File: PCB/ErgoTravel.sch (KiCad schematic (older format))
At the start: 63 parts, among them J1 Conn_01x03, J2 Audio-Jack-4, J3 Audio-Jack-4, K1 KEYSW, K10 KEYSW, K11 KEYSW, K12 KEYSW, K13 KEYSW, K14 KEYSW, K15 KEYSW, K16 KEYSW, K17 KEYSW, K18 KEYSW, K19 KEYSW, K2 KEYSW, K20 KEYSW, K21 KEYSW, K22 KEYSW, K23 KEYSW, K24 KEYSW, K25 KEYSW, K26 KEYSW, K27 KEYSW, K28 KEYSW, K3 KEYSW, K4 KEYSW, K5 KEYSW, K6 KEYSW, K7 KEYSW, K8 KEYSW, K9 KEYSW, SW1 SW_PUSH, SW2 SW_PUSH, U1 ProMicro

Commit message: Adding internal Plates
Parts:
- added J4: Conn_01x06, footprints:ICSP-Header, symbol Conn_01x06
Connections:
- net labels added: MISO, MOSI, RESET, SCK
- wire segments 172 -> 186
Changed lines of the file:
@@
 LIBS:keyboard_parts
 LIBS:canadian_parts
+LIBS:ErgoTravel-cache
 EELAYER 25 0
 EELAYER END
@@
 L GND #PWR06
 U 1 1 5A9D5401
-P 7100 4700
-F 0 "#PWR06" H 7100 4450 50  0001 C CNN
-F 1 "GND" H 7100 4550 50  0000 C CNN
-F 2 "" H 7100 4700 50  0001 C CNN
-F 3 "" H 7100 4700 50  0001 C CNN
-	1    7100 4700
+P 7350 4200
+F 0 "#PWR06" H 7350 3950 50  0001 C CNN
+F 1 "GND" H 7350 4050 50  0000 C CNN
+F 2 "" H 7350 4200 50  0001 C CNN
+F 3 "" H 7350 4200 50  0001 C CNN
+	1    7350 4200
 	0    1    1    0
 $EndComp
@@
 L GND #PWR07
 U 1 1 5A9D54C0
-P 7100 5850
-F 0 "#PWR07" H 7100 5600 50  0001 C CNN
-F 1 "GND" H 7100 5700 50  0000 C CNN
-F 2 "" H 7100 5850 50  0001 C CNN
-F 3 "" H 7100 5850 50  0001 C CNN
-	1    7100 5850
+P 7400 5400
+F 0 "#PWR07" H 7400 5150 50  0001 C CNN
+F 1 "GND" H 7400 5250 50  0000 C CNN
+F 2 "" H 7400 5400 50  0001 C CNN
+F 3 "" H 7400 5400 50  0001 C CNN
+	1    7400 5400
 	0    1    1    0
 $EndComp
@@
 L VCC #PWR08
 U 1 1 5A9D557F
-P 7100 4600
-F 0 "#PWR08" H 7100 4450 50  0001 C CNN
-F 1 "VCC" H 7100 4750 50  0000 C CNN
-F 2 "" H 7100 4600 50  0001 C CNN
-F 3 "" H 7100 4600 50  0001 C CNN
-	1    7100 4600
+P 7350 4800
+F 0 "#PWR08" H 7350 4650 50  0001 C CNN
+F 1 "VCC" H 7350 4950 50  0000 C CNN
+F 2 "" H 7350 4800 50  0001 C CNN
+F 3 "" H 7350 4800 50  0001 C CNN
+	1    7350 4800
 	0    -1   -1   0
 $EndComp
@@
 L VCC #PWR09
 U 1 1 5A9D563E
-P 7100 5750
-F 0 "#PWR09" H 7100 5600 50  0001 C CNN
-F 1 "VCC" H 7100 5900 50  0000 C CNN
-F 2 "" H 7100 5750 50  0001 C CNN
-F 3 "" H 7100 5750 50  0001 C CNN
-	1    7100 5750
-	0    -1   -1   0
-$EndComp
-Text GLabel 7350 4200 0    60   Input ~ 0
+P 7350 5950
+F 0 "#PWR09" H 7350 5800 50  0001 C CNN
+F 1 "VCC" H 7350 6100 50  0000 C CNN
+F 2 "" H 7350 5950 50  0001 C CNN
+F 3 "" H 7350 5950 50  0001 C CNN
+	1    7350 5950
+	0    -1   -1   0
+$EndComp
+Text GLabel 7100 4600 0    60   Input ~ 0
 sda
-Text GLabel 7400 5400 0    60   Input ~ 0
+Text GLabel 7100 5750 0    60   Input ~ 0
 sda
-Text GLabel 7350 4800 0    60   Input ~ 0
+Text GLabel 7100 4700 0    60   Input ~ 0
 scl
-Text GLabel 7350 5950 0    60   Input ~ 0
+Text GLabel 7100 5850 0    60   Input ~ 0
 scl
 $Comp
@@
 Wire Wire Line
 	5350 4650 5650 4650
+$Comp
+L Conn_01x06 J4
+U 1 1 5ABA3EE2
+P 4050 4600
+F 0 "J4" H 4050 4900 50  0000 C CNN
+F 1 "Conn_01x06" H 4050 4200 50  0000 C CNN
+F 2 "footprints:ICSP-Header" H 4050 4600 50  0001 C CNN
+F 3 "" H 4050 4600 50  0001 C CNN
+	1    4050 4600
+	1    0    0    -1
+$EndComp
+$Comp
+L VCC #PWR014
+U 1 1 5ABA3FE3
+P 3750 4500
+F 0 "#PWR014" H 3750 4350 50  0001 C CNN
+F 1 "VCC" H 3750 4650 50  0000 C CNN
+F 2 "" H 3750 4500 50  0001 C CNN
+F 3 "" H 3750 4500 50  0001 C CNN
+	1    3750 4500
+	0    -1   -1   0
+$EndComp
+$Comp
+L GND #PWR015
+U 1 1 5ABA4377
+P 3750 4900
+F 0 "#PWR015" H 3750 4650 50  0001 C CNN
+F 1 "GND" H 3750 4750 50  0000 C CNN
+F 2 "" H 3750 4900 50  0001 C CNN
+F 3 "" H 3750 4900 50  0001 C CNN
+	1    3750 4900
+	0    1    1    0
+$EndComp
+Text GLabel 3500 4800 0    60   Input ~ 0
+RESET
+Text GLabel 4850 5250 2    60   Input ~ 0
+RESET
+Wire Wire Line
+	4850 5250 4500 5250
+Wire Wire Line
+	4500 5250 4500 5700
+Connection ~ 4500 5700
+Wire Wire Line
+	3750 4900 3850 4900
+Wire Wire Line
+	3850 4800 3500 4800
+Wire Wire Line
+	3750 4500 3850 4500
+Text GLabel 3550 4400 0    60   Input ~ 0
+MISO
+Text GLabel 3550 4600 0    60   Input ~ 0
+SCK
+Text GLabel 3550 4700 0    60   Input ~ 0
+MOSI
+Text GLabel 4000 6800 2    60   Input ~ 0
+SCK
+Text GLabel 4000 6950 2    60   Input ~ 0
+MOSI
+Text GLabel 4000 7100 2    60   Input ~ 0
+MISO
+Wire Wire Line
+	4000 6800 3900 6800
+Wire Wire Line
+	3900 6800 3900 6300
+Connection ~ 3900 6300
+Wire Wire Line
+	4000 6950 3850 6950
+Wire Wire Line
+	3850 6950 3850 6500
+Connection ~ 3850 6500
+Wire Wire Line
+	4000 7100 3800 7100
+Wire Wire Line
+	3800 7100 3800 6400
+Connection ~ 3800 6400
+Wire Wire Line
+	3550 4700 3850 4700
+Wire Wire Line
+	3850 4600 3550 4600
+Wire Wire Line
+	3550 4400 3850 4400
 $EndSCHEMATC

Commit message: moved D13
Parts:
- R1, R2: footprint Resistors_Universal:Resistor_SMD+THTuniversal_0805to1206_RM10_HandSoldering_RevA_Date25Jun2010 -> Resistors_THT:R_Axial_DIN0207_L6.3mm_D2.5mm_P10.16mm_Horizontal
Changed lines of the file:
@@
 F 0 "R1" V 9780 4600 50  0000 C CNN
 F 1 "4.7k" V 9700 4600 50  0000 C CNN
-F 2 "Resistors_Universal:Resistor_SMD+THTuniversal_0805to1206_RM10_HandSoldering_RevA_Date25Jun2010" V 9630 4600 50  0001 C CNN
+F 2 "Resistors_THT:R_Axial_DIN0207_L6.3mm_D2.5mm_P10.16mm_Horizontal" V 9630 4600 50  0001 C CNN
 F 3 "" H 9700 4600 50  0001 C CNN
 	1    9700 4600
@@
 F 0 "R2" V 10380 4600 50  0000 C CNN
 F 1 "4.7k" V 10300 4600 50  0000 C CNN
-F 2 "Resistors_Universal:Resistor_SMD+THTuniversal_0805to1206_RM10_HandSoldering_RevA_Date25Jun2010" V 10230 4600 50  0001 C CNN
+F 2 "Resistors_THT:R_Axial_DIN0207_L6.3mm_D2.5mm_P10.16mm_Horizontal" V 10230 4600 50  0001 C CNN
 F 3 "" H 10300 4600 50  0001 C CNN
 	1    10300 4600

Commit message: V1.01 PCB and Plates incl Gerbers
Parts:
- removed J1: Conn_01x03, Pin_Headers:Pin_Header_Straight_1x03_Pitch2.54mm, symbol Conn_01x03
- added J1: Conn_01x05, Pin_Headers:Pin_Header_Angled_1x05_Pitch2.54mm, symbol Conn_01x05
- added J10, J11, J12, J5, J6, J7, J8, J9: Conn_01x01, Mounting_Holes:MountingHole_2.2mm_M2_DIN965, symbol Conn_01x01
- added SJ1: SOLDER_JUMPER, footprints:SolderJumperSingle, symbol SOLDER_JUMPER
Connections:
- net labels added: RX, sdaPM
- wire segments 186 -> 193
- no-connect marks 4 -> 3
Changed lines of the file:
@@
 row3
 Text GLabel 2500 5900 0    60   Input ~ 0
-sda
+sdaPM
 Text GLabel 2500 6000 0    60   Input ~ 0
 scl
@@
 	10300 4900 10300 4750
 NoConn ~ 2750 6100
-NoConn ~ 2750 5600
 Wire Wire Line
 	2500 6200 2750 6200
@@
 $EndComp
 $Comp
-L Conn_01x03 J1
-U 1 1 5A9D90E9
-P 5850 4750
-F 0 "J1" H 5850 4950 50  0000 C CNN
-F 1 "Conn_01x03" H 5850 4550 50  0000 C CNN
-F 2 "Pin_Headers:Pin_Header_Straight_1x03_Pitch2.54mm" H 5850 4750 50  0001 C CNN
-F 3 "" H 5850 4750 50  0001 C CNN
-	1    5850 4750
-	1    0    0    -1
-$EndComp
-$Comp
 L Audio-Jack-4 J3
 U 1 1 5A9D9202
@@
 L GND #PWR013
 U 1 1 5A9DC92B
-P 5400 4850
-F 0 "#PWR013" H 5400 4600 50  0001 C CNN
-F 1 "GND" H 5400 4700 50  0000 C CNN
-F 2 "" H 5400 4850 50  0001 C CNN
-F 3 "" H 5400 4850 50  0001 C CNN
-	1    5400 4850
+P 5375 5050
+F 0 "#PWR013" H 5375 4800 50  0001 C CNN
+F 1 "GND" H 5375 4900 50  0000 C CNN
+F 2 "" H 5375 5050 50  0001 C CNN
+F 3 "" H 5375 5050 50  0001 C CNN
+	1    5375 5050
 	0    1    1    0
 $EndComp
@@
 Wire Wire Line
 	3550 4400 3850 4400
+Text GLabel 5205 6320 0    60   Input ~ 0
+sdaPM
+$Comp
+L SOLDER_JUMPER SJ1
+U 1 1 5ACEEE8B
+P 5380 6370
+F 0 "SJ1" H 5380 6320 60  0000 C CNN
+F 1 "SOLDER_JUMPER" H 5430 6520 60  0001 C CNN
+F 2 "footprints:SolderJumperSingle" H 5430 6370 60  0001 C CNN
+F 3 "" H 5430 6370 60  0000 C CNN
+	1    5380 6370
+	1    0    0    -1
+$EndComp
+Wire Wire Line
+	5205 6320 5280 6320
+Text GLabel 5670 6325 2    60   Input ~ 0
+sda
+Wire Wire Line
+	5670 6325 5570 6325
+Wire Wire Line
+	5570 6325 5570 6320
+Wire Wire Line
+	5570 6320 5530 6320
+Text GLabel 2505 5600 0    60   Input ~ 0
+RX
+Wire Wire Line
+	2505 5600 2750 5600
+$Comp
+L Conn_01x05 J1
+U 1 1 5ACF0B02
+P 5850 4850
+F 0 "J1" H 5850 5150 50  0000 C CNN
+F 1 "Conn_01x05" H 5850 4550 50  0000 C CNN
+F 2 "Pin_Headers:Pin_Header_Angled_1x05_Pitch2.54mm" H 5850 4850 50  0001 C CNN
+F 3 "" H 5850 4850 50  0001 C CNN
+	1    5850 4850
+	1    0    0    -1
+$EndComp
+Text GLabel 5375 4950 0    60   Input ~ 0
+RESET
+Text GLabel 5400 4850 0    60   Input ~ 0
+RX
+Wire Wire Line
+	5375 4950 5650 4950
+Wire Wire Line
+	5375 5050 5650 5050
+$Comp
+L Conn_01x01 J8
+U 1 1 5ACF1FC6
+P 1055 4410
+F 0 "J8" H 1055 4510 50  0000 C CNN
+F 1 "Conn_01x01" H 1055 4310 50  0000 C CNN
+F 2 "Mounting_Holes:MountingHole_2.2mm_M2_DIN965" H 1055 4410 50  0001 C CNN
+F 3 "" H 1055 4410 50  0001 C CNN
+	1    1055 4410
+	1    0    0    -1
+$EndComp
+$Comp
+L Conn_01x01 J7
+U 1 1 5ACF217B
+P 1050 4725
+F 0 "J7" H 1050 4825 50  0000 C CNN
+F 1 "Conn_01x01" H 1050 4625 50  0000 C CNN
+F 2 "Mounting_Holes:MountingHole_2.2mm_M2_DIN965" H 1050 4725 50  0001 C CNN
+F 3 "" H 1050 4725 50  0001 C CNN
+	1    1050 4725
+	1    0    0    -1
+$EndComp
+$Comp
+L Conn_01x01 J6
+U 1 1 5ACF22A6
+P 1040 5035
+F 0 "J6" H 1040 5135 50  0000 C CNN
+F 1 "Conn_01x01" H 1040 4935 50  0000 C CNN
+F 2 "Mounting_Holes:MountingHole_2.2mm_M2_DIN965" H 1040 5035 50  0001 C CNN
+F 3 "" H 1040 5035 50  0001 C CNN
+	1    1040 5035
+	1    0    0    -1
+$EndComp
+$Comp
+L Conn_01x01 J5
+U 1 1 5ACF2404
+P 1030 5340
+F 0 "J5" H 1030 5440 50  0000 C CNN
+F 1 "Conn_01x01" H 1030 5240 50  0000 C CNN
+F 2 "Mounting_Holes:MountingHole_2.2mm_M2_DIN965" H 1030 5340 50  0001 C CNN
+F 3 "" H 1030 5340 50  0001 C CNN
+	1    1030 5340
+	1    0    0    -1
+$EndComp
+$Comp
+L Conn_01x01 J9
+U 1 1 5ACF2596
+P 1570 4405
+F 0 "J9" H 1570 4505 50  0000 C CNN
+F 1 "Conn_01x01" H 1570 4305 50  0000 C CNN
+F 2 "Mounting_Holes:MountingHole_2.2mm_M2_DIN965" H 1570 4405 50  0001 C CNN
+F 3 "" H 1570 4405 50  0001 C CNN
+	1    1570 4405
+	1    0    0    -1
+$EndComp
+$Comp
+L Conn_01x01 J10
+U 1 1 5ACF2748
+P 1580 4725
+F 0 "J10" H 1580 4825 50  0000 C CNN
+F 1 "Conn_01x01" H 1580 4625 50  0000 C CNN
+F 2 "Mounting_Holes:MountingHole_2.2mm_M2_DIN965" H 1580 4725 50  0001 C CNN
+F 3 "" H 1580 4725 50  0001 C CNN
+	1    1580 4725
+	1    0    0    -1
+$EndComp
+$Comp
+L Conn_01x01 J12
+U 1 1 5ACF2887
+P 1595 5030
+F 0 "J12" H 1595 5130 50  0000 C CNN
+F 1 "Conn_01x01" H 1595 4930 50  0000 C CNN
+F 2 "Mounting_Holes:MountingHole_2.2mm_M2_DIN965" H 1595 5030 50  0001 C CNN
+F 3 "" H 1595 5030 50  0001 C CNN
+	1    1595 5030
+	1    0    0    -1
+$EndComp
+$Comp
+L Conn_01x01 J11
+U 1 1 5ACF29E3
+P 1580 5360
+F 0 "J11" H 1580 5460 50  0000 C CNN
+F 1 "Conn_01x01" H 1580 5260 50  0000 C CNN
+F 2 "Mounting_Holes:MountingHole_2.2mm_M2_DIN965" H 1580 5360 50  0001 C CNN
+F 3 "" H 1580 5360 50  0001 C CNN
+	1    1580 5360
+	1    0    0    -1
+$EndComp
 $EndSCHEMATC

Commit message: initial V1.02 files and 3d printed case folders
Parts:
- J1: footprint Pin_Headers:Pin_Header_Angled_1x05_Pitch2.54mm -> Pin_Headers:Pin_Header_Straight_1x05_Pitch2.54mm
- SJ1: footprint footprints:SolderJumperSingle -> footprints:SolderJumperSingle-largepads
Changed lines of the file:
@@
 F 0 "SJ1" H 5380 6320 60  0000 C CNN
 F 1 "SOLDER_JUMPER" H 5430 6520 60  0001 C CNN
-F 2 "footprints:SolderJumperSingle" H 5430 6370 60  0001 C CNN
+F 2 "footprints:SolderJumperSingle-largepads" H 5430 6370 60  0001 C CNN
 F 3 "" H 5430 6370 60  0000 C CNN
 	1    5380 6370
@@
 F 0 "J1" H 5850 5150 50  0000 C CNN
 F 1 "Conn_01x05" H 5850 4550 50  0000 C CNN
-F 2 "Pin_Headers:Pin_Header_Angled_1x05_Pitch2.54mm" H 5850 4850 50  0001 C CNN
+F 2 "Pin_Headers:Pin_Header_Straight_1x05_Pitch2.54mm" H 5850 4850 50  0001 C CNN
 F 3 "" H 5850 4850 50  0001 C CNN
 	1    5850 4850

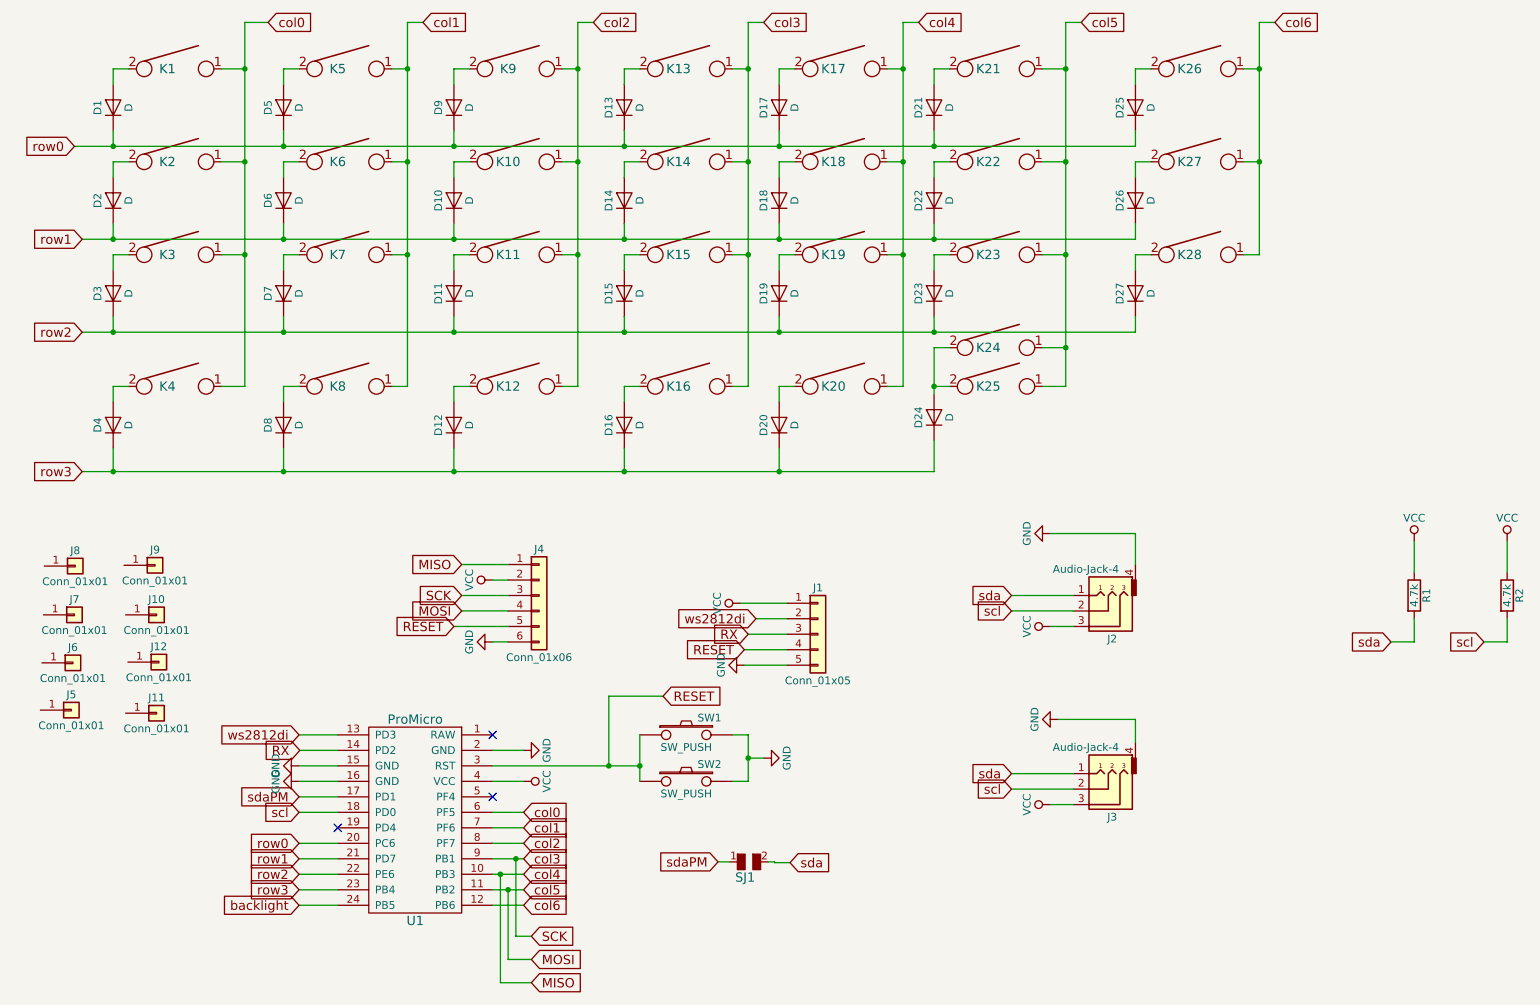
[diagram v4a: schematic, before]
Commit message: Updating Internal Plates with Alps/MX Openings
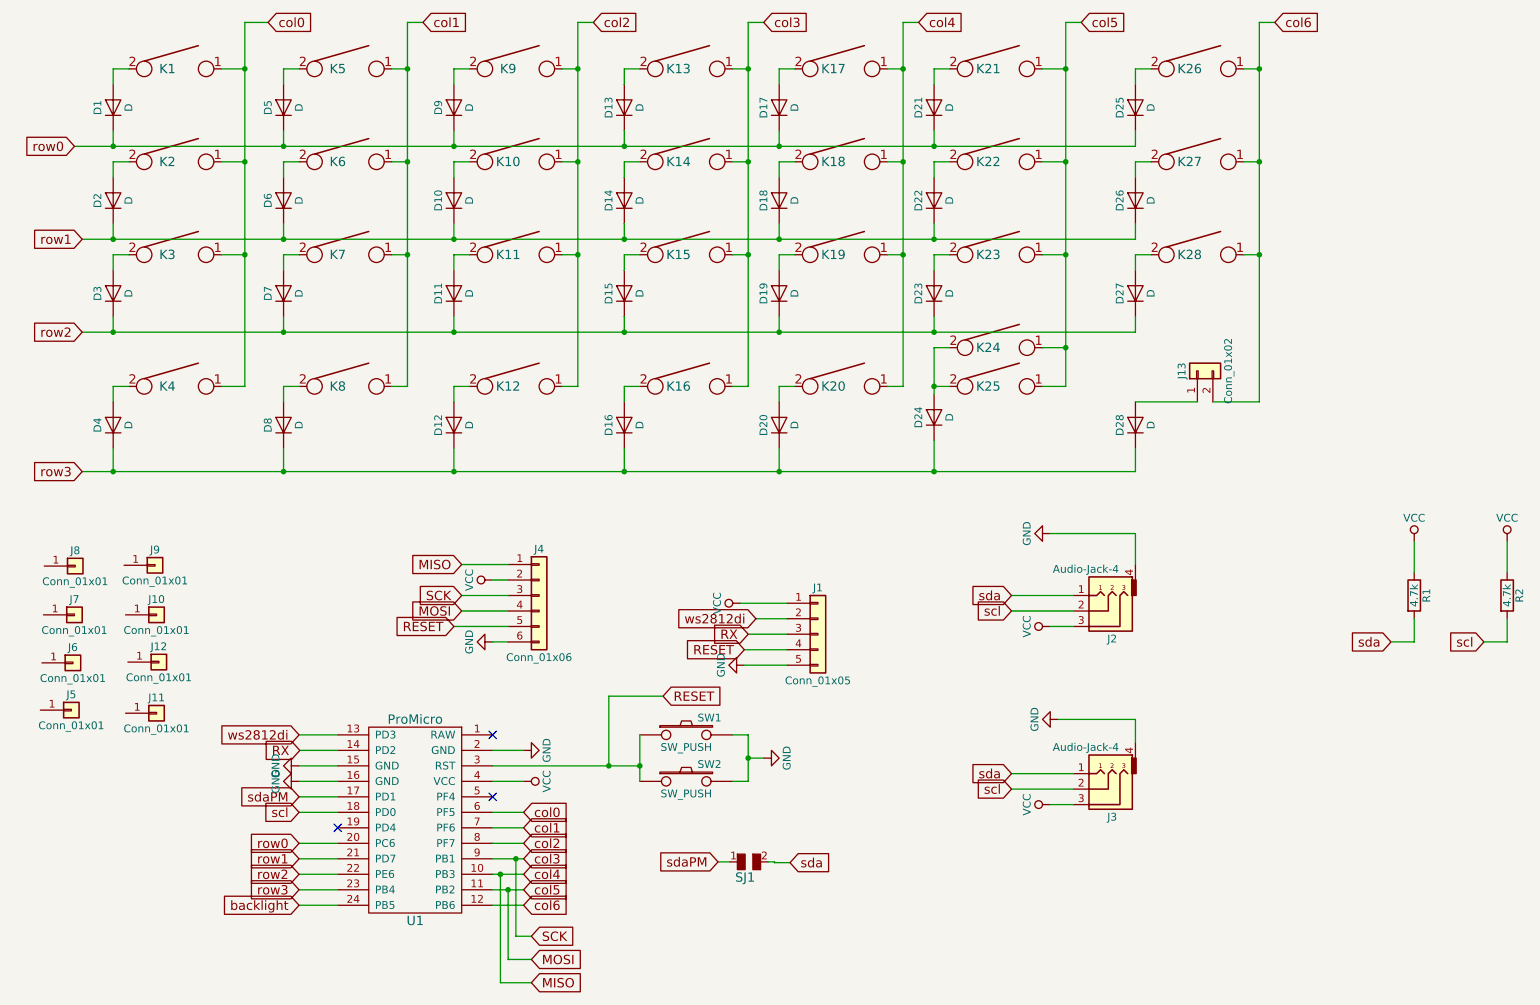
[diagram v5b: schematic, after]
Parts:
- added D28: D, footprints:D_SOD123_axial-dual, symbol D
- added J13: Conn_01x02, Pin_Headers:Pin_Header_Straight_1x02_Pitch2.54mm, symbol Conn_01x02
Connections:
- net col6: now also J13.2 (Pin_2)
- net row3: now also D28.1 (K)
- new net: D28.2 (A), J13.1 (Pin_1)
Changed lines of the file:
@@
 	8600 2400 8700 2400
 Wire Wire Line
-	8700 2400 8700 900
+	8700 900  8700 3350
 Wire Wire Line
 	8700 900  8800 900
@@
 	6600 3600 6600 3800
 Wire Wire Line
-	6600 3800 1100 3800
+	7900 3800 1100 3800
 Wire Wire Line
 	6600 1600 6600 1700
@@
 	1    0    0    -1
 $EndComp
+$Comp
+L Conn_01x02 J13
+U 1 1 5B0466BE
+P 8300 3150
+F 0 "J13" H 8300 3250 50  0000 C CNN
+F 1 "Conn_01x02" H 8300 2950 50  0000 C CNN
+F 2 "Pin_Headers:Pin_Header_Straight_1x02_Pitch2.54mm" H 8300 3150 50  0001 C CNN
+F 3 "" H 8300 3150 50  0001 C CNN
+	1    8300 3150
+	0    -1   -1   0
+$EndComp
+Wire Wire Line
+	8700 3350 8400 3350
+Connection ~ 8700 2400
+$Comp
+L D D28
+U 1 1 5B04698B
+P 7900 3500
+F 0 "D28" H 7900 3600 50  0000 C CNN
+F 1 "D" H 7900 3400 50  0000 C CNN
+F 2 "footprints:D_SOD123_axial-dual" H 7900 3500 50  0001 C CNN
+F 3 "" H 7900 3500 50  0001 C CNN
+	1    7900 3500
+	0    -1   -1   0
+$EndComp
+Wire Wire Line
+	7900 3650 7900 3800
+Connection ~ 6600 3800
+Wire Wire Line
+	7900 3350 8300 3350
 $EndSCHEMATC

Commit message: Changing Adding priotities to Acrylic Case items
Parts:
- added J14: Conn_01x02, Pin_Headers:Pin_Header_Straight_1x02_Pitch2.54mm, symbol Conn_01x02
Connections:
- net GND: now also J14.1 (Pin_1)
- net RAW: now reaches U1.1 (RAW)
- net RAW: now also J14.2 (Pin_2)
- no-connect marks 3 -> 2
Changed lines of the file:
@@
 	2750 5500 2500 5500
 NoConn ~ 3750 5900
-NoConn ~ 3750 5500
 Text GLabel 2500 5500 0    60   Input ~ 0
 ws2812di
@@
 Wire Wire Line
 	7900 3350 8300 3350
+$Comp
+L Conn_01x02 J14
+U 1 1 5B22F995
+P 9750 3150
+F 0 "J14" H 9750 3250 50  0000 C CNN
+F 1 "Conn_01x02" H 9750 2950 50  0000 C CNN
+F 2 "Pin_Headers:Pin_Header_Straight_1x02_Pitch2.54mm" H 9750 3150 50  0001 C CNN
+F 3 "" H 9750 3150 50  0001 C CNN
+	1    9750 3150
+	0    -1   -1   0
+$EndComp
+Wire Wire Line
+	3750 5500 3950 5500
+Text Label 3950 5500 0    60   ~ 0
+RAW
+Wire Wire Line
+	9850 3350 9850 3550
+Text Label 9850 3550 0    60   ~ 0
+RAW
+$Comp
+L GND #PWR016
+U 1 1 5B230418
+P 9750 3450
+F 0 "#PWR016" H 9750 3200 50  0001 C CNN
+F 1 "GND" H 9750 3300 50  0000 C CNN
+F 2 "" H 9750 3450 50  0001 C CNN
+F 3 "" H 9750 3450 50  0001 C CNN
+	1    9750 3450
+	1    0    0    -1
+$EndComp
+Wire Wire Line
+	9750 3450 9750 3350
 $EndSCHEMATC
